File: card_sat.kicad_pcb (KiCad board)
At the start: 2 copper layers, 115 x 127 mm, 24 parts, among them J1 Conn_01x05_Male, J2 Conn_01x05_Male, J3 Conn_01x05_Male, J4 Conn_01x05_Male, J5 Conn_01x04_Male, U1 ATtiny85-20P, U2 ATtiny85-20P, U3 ATtiny85-20P

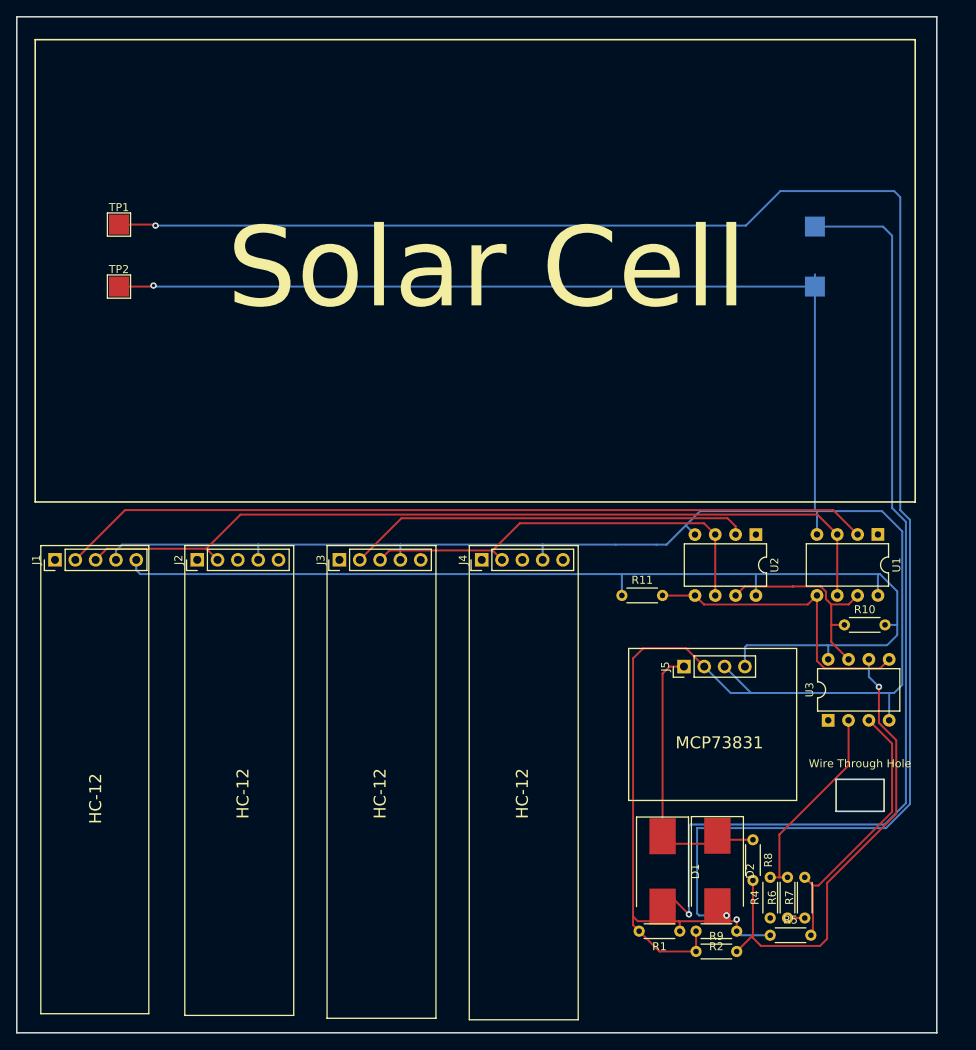
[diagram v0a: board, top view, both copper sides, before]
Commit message: changed schematic to use pico
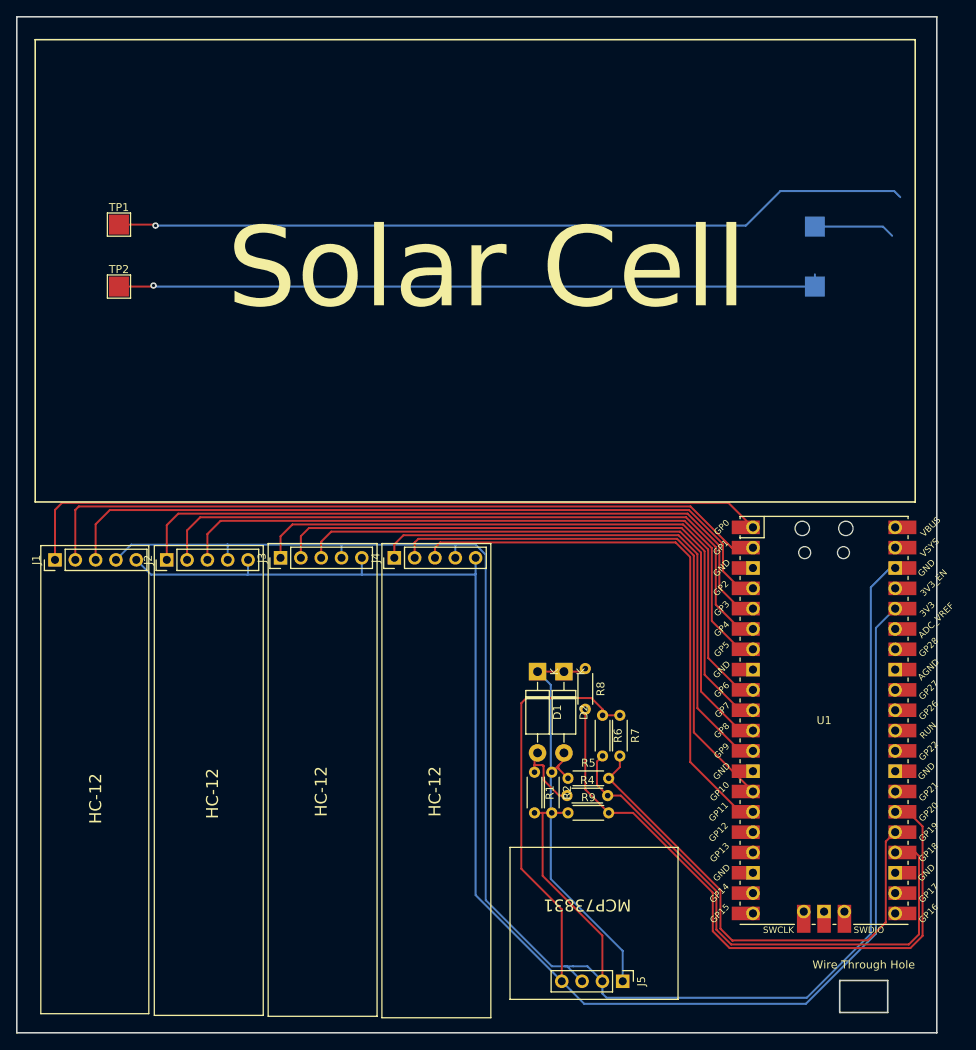
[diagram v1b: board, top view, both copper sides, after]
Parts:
- removed R10, R11: 10k, Resistor_THT:R_Axial_DIN0204_L3.6mm_D1.6mm_P5.08mm_Horizontal
- removed U2, U3: ATtiny85-20P, Package_DIP:DIP-8_W7.62mm
- D1, D2: value B340 -> 1N5819; footprint Diode_SMD:D_SMC_Handsoldering -> Diode_THT:D_DO-41_SOD81_P10.16mm_Horizontal
- U1: value ATtiny85-20P -> Pico; footprint Package_DIP:DIP-8_W7.62mm -> MCU_RaspberryPi_and_Boards:RPi_Pico_SMD_TH
- moved J5 40.1 mm to (135.7, 140.6), turned to -90 degrees
- moved R7 34.3 mm to (135.4, 107.3), turned to -90 degrees
- moved R6 34.3 mm to (133.2, 107.3), turned to -90 degrees
- moved R5 32.0 mm to (128.9, 115.2)
- moved D2 31.4 mm to (128.4, 101.9)
- moved R2 30.5 mm to (126.9, 114.4), turned to -90 degrees
- moved R8 29.9 mm to (131.1, 101.5)
- moved R4 29.7 mm to (128.8, 117.3), turned to 0 degrees
- moved D1 29.5 mm to (125.1, 101.9)
- moved R1 26.9 mm to (124.7, 114.4), turned to -90 degrees
- moved U1 24.2 mm to (160.9, 108.0), turned to 0 degrees
- moved R9 23.6 mm to (128.9, 119.5)
- moved J4 10.9 mm to (107.2, 87.6)
- moved J3 7.37 mm to (93.0, 87.6)
- moved J2 3.81 mm to (78.7, 87.9)
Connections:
- J1 pad 1: unconnected-(J1-Pad1) -> SET1
- J1 pad 2: RXD1 -> TXD1
- J2 pad 1: unconnected-(J2-Pad1) -> SET2
- J2 pad 2: RXD1 -> TXD2
- J3 pad 1: unconnected-(J3-Pad1) -> SET3
- J3 pad 2: RXD3 -> TXD3
- J4 pad 1: unconnected-(J4-Pad1) -> SET4
- J4 pad 2: RXD3 -> TXD4
- R6 pad 1: VREF1 -> VCC
- R7 pad 1: VREF1 -> VCC
- U1 pad 1: unconnected-(U1-Pad1) -> SET1
- U1 pad 2: RXD1 -> TXD1
- U1 pad 3: RXD1 -> unconnected-(U1-Pad3)
- U1 pad 4: GND -> RXD1
- U1 pad 5: SDA -> SET2
- U1 pad 6: RXD1 -> TXD2
- U1 pad 7: SCK -> RXD2
- U1 pad 8: VCC -> unconnected-(U1-Pad8)
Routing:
- net GND: track 705.8 -> 320.6 mm, vias 4 -> 1
- net VREF1: track 38.1 -> 159.8 mm, vias 0 -> 1
- net RXD1: track 207.9 -> 93.4 mm
- net VCC: track 136.5 -> 241.1 mm
- net SET1: track 0.00 -> 95.1 mm
- net TXD1: track 0.00 -> 93.3 mm
- net SET2: track 0.00 -> 86.2 mm
- net TXD2: track 0.00 -> 85.1 mm
- net RXD2: track 0.00 -> 84.1 mm
- net SET3: track 0.00 -> 78.9 mm
- net TXD3: track 0.00 -> 78.1 mm
- net TXD4: track 0.00 -> 70.4 mm
- net RXD4: track 0.00 -> 70.2 mm
- net SET4: track 0.00 -> 69.4 mm
- net Net-(R4-Pad2): track 25.4 -> 68.7 mm
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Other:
- outline, holes or cut-outs redrawn

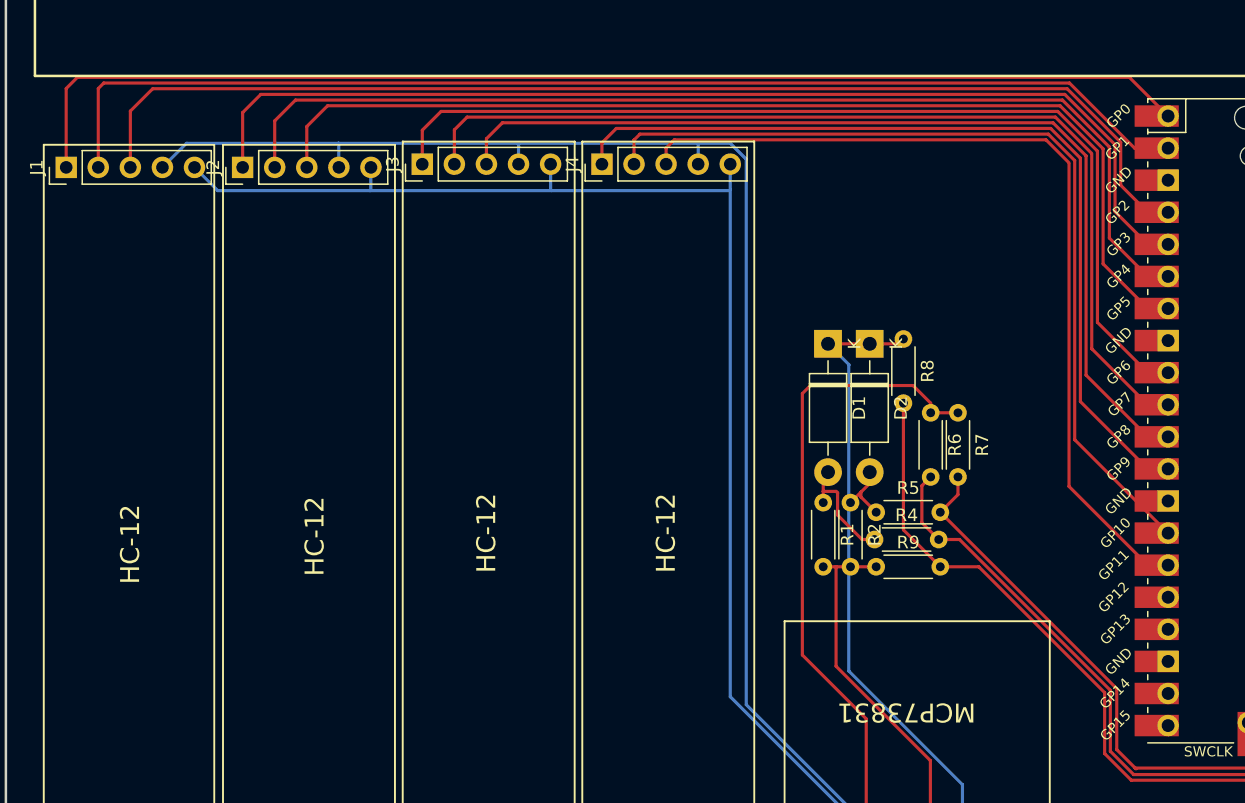
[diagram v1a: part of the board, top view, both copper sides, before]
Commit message: switched to python
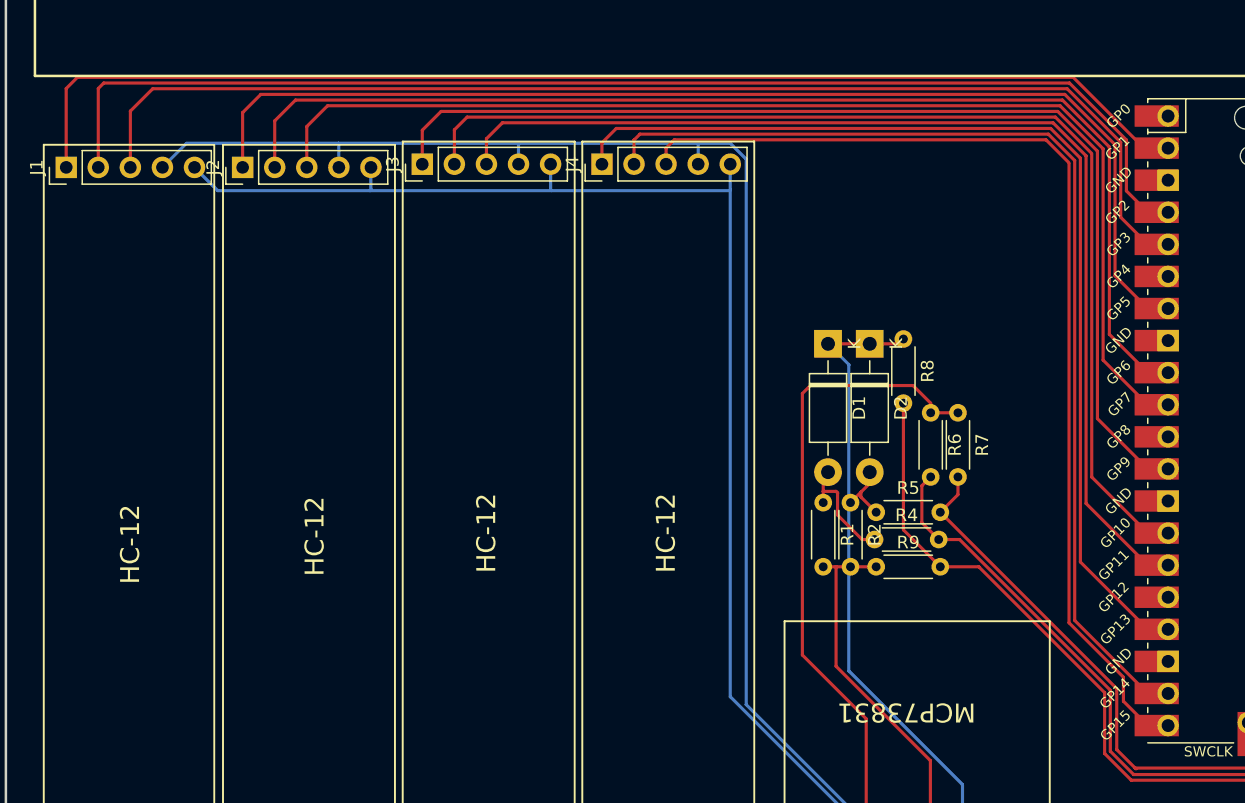
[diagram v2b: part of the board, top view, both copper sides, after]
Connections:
- R6 pad 1: VCC -> VREF1
- R7 pad 1: VCC -> VREF1
- U1 pad 1: SET1 -> unconnected-(U1-Pad1)
- U1 pad 10: TXD3 -> RXD2
- U1 pad 11: RXD3 -> unconnected-(U1-Pad11)
- U1 pad 12: SET4 -> SET3
- U1 pad 14: TXD4 -> TXD3
- U1 pad 15: RXD4 -> RXD3
- U1 pad 17: unconnected-(U1-Pad17) -> SET4
- U1 pad 19: unconnected-(U1-Pad19) -> TXD4
- U1 pad 2: TXD1 -> SET1
- U1 pad 20: unconnected-(U1-Pad20) -> RXD4
- U1 pad 4: RXD1 -> TXD1
- U1 pad 5: SET2 -> RXD1
- U1 pad 6: TXD2 -> unconnected-(U1-Pad6)
- U1 pad 7: RXD2 -> SET2
- U1 pad 9: SET3 -> TXD2
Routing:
- net GND: track 320.6 -> 375.6 mm
- net VREF1: track 159.8 -> 109.9 mm
- net TXD4: track 70.4 -> 84.1 mm
- net RXD4: track 70.2 -> 82.9 mm
- net SET4: track 69.4 -> 82.1 mm
- net TXD3: track 78.1 -> 88.2 mm
- net RXD3: track 77.0 -> 87.1 mm
- net RXD2: track 84.1 -> 91.7 mm
- net TXD2: track 85.1 -> 92.7 mm
- net SET3: track 78.9 -> 86.5 mm
- net PANEL2: track 5.13 -> 0.00 mm
- net SET2: track 86.2 -> 91.3 mm
- net TXD1: track 93.3 -> 97.7 mm
- net RXD1: track 93.4 -> 95.9 mm
- net unconnected-(U1-Pad6): track 0.00 -> 1.61 mm
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
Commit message: debugging still :(
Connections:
- U1 pad 24: Net-(R4-Pad2) -> unconnected-(U1-Pad24)
- U1 pad 25: Net-(R5-Pad2) -> unconnected-(U1-Pad25)
- U1 pad 26: Net-(R8-Pad2) -> unconnected-(U1-Pad26)
- U1 pad 31: unconnected-(U1-Pad31) -> Net-(R4-Pad2)
- U1 pad 32: unconnected-(U1-Pad32) -> Net-(R5-Pad2)
- U1 pad 34: unconnected-(U1-Pad34) -> Net-(R8-Pad2)
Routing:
- net Net-(R8-Pad2): track 81.7 -> 102.0 mm
- net Net-(R4-Pad2): track 68.7 -> 86.0 mm
- net Net-(R5-Pad2): track 64.2 -> 79.9 mm
- net unconnected-(U1-Pad25): track 0.00 -> 2.09 mm
- net unconnected-(U1-Pad26): track 0.00 -> 1.61 mm
